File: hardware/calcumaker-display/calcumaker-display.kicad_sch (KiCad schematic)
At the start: 0 parts

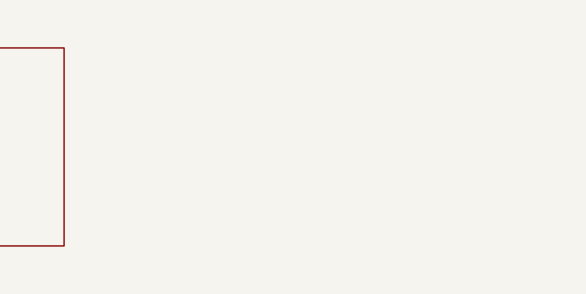
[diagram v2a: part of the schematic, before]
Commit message: Error handling: HP-style glass codes + DNP-optional aux OLED (display board)
Two layers, per design discussion:

ENGINE/APP — CalcError restructured: TypeError(&str) becomes Op(code, msg)
with class constructors at every site; code() gives the HP-16C-style glass
class (0 math domain, 1 register/flag, 2 bits/shift/word, 3 mode ranges,
4 too large, 5 no solution, 6 stack/entry, 7 dates, 8 statistics, 9 reserved
for crash recovery), text() the full string. App shows a transient 'Error N'
on the X row (cleared by the next key, like SHOW) and keeps the full text on
the status line — the duplicated error-string mapping in run_owned/flush is
now one report() helper. All of 'Error N' renders on the 7-seg. 211 tests.

HARDWARE — the aux OLED lands on the DISPLAY board (user decision): new
AuxDisplay sheet with J2, a 1x4 socket (PZ254V-11-04P C2691448) receiving a
standard 0.91in SSD1306 128x32 I2C module, DNP by default, hand-placed with
the THT digits. Interconnect grows 1x8 -> 1x10 (PZ254V-11-10P C492409, both
boards, pinout now ... 8=+3V3 9=SDA 10=SCL); I2C pull-ups R14/R15 4.7k on
the main board, DNP with the OLED. Both boards regenerate + check clean
(main 161, display 22 components). DESIGN.md documents the layered error
story and names the reusable 'DNP-optional aux' pattern; PARTS.md updated.

Co-Authored-By: Claude Fable 5 <noreply@anthropic.com>
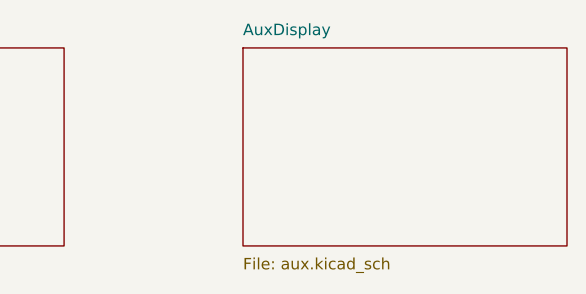
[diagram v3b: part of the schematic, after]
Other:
- added sheet AuxDisplay (aux.kicad_sch)
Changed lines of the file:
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@@
+		)
+	)
+	(sheet
+		(at 152.40 40.64)
+		(size 36.00 22.00)
+		(fields_autoplaced yes)
+		(stroke (width 0.1524) (type solid))
+		(fill (color 0 0 0 0.0000))
+		(property "Sheetname" "AuxDisplay"
+			(at 152.40 39.37 0)
+			(effects (font (size 1.27 1.27)) (justify left bottom))
+		)
+		(property "Sheetfile" "aux.kicad_sch"
+			(at 152.40 63.91 0)
+			(effects (font (size 1.27 1.27)) (justify left top))
 		)
 	)

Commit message: hardware: 3-board split (MCU + keyboard + display), wired display, real connectors
Split the single logic board into three, wire the display as a KiCad
multi-channel design, and settle every interconnect on real, in-stock parts.

Three-board split (was two):
- Rename calcumaker-main -> calcumaker-mcu (brain/PSU logic board).
- New calcumaker-keyboard board: 50-key Cherry MX matrix + its own
  STM32G031K8U6 scanner (LCSC C432207, UFQFPN-32) + annunciator LEDs,
  mezzanine-stacked above the MCU board. Keyscanning is off the main board;
  only an I2C + UART link + KB_IRQ wake + power cross the mezzanine.

Display board (calcumaker-display):
- Corrected FJ5161AH to a SINGLE-digit 0.56" common-cathode part (C8093) --
  it is NOT a 4-digit module; 48 single digits (16/row x 3), authored symbol
  + 0.56" LTS6760 land. The old 4-digit CC56-12 mapping (and its 3D model)
  was the phantom "clock colon".
- Rebuilt as a KiCad multi-channel design: one reusable display_row.kicad_sch
  (1 TM1640 + 16 digits, fully wired) instantiated x3. Extended kschgen.py
  with wiring primitives + reused-sheet (multi-channel) support.

Connectors (real, verified LCSC / DigiKey parts):
- Display link -> 0.5mm 12P FFC: AFC01-S12FCA-00 (LCSC C262661) on both
  boards; cable = GCT FFC05-TIN 05-12-A-<len>-A-4-06-4-T (DigiKey accessory,
  length TBD). +5V/GND conductors doubled for the display LED current.
- Keyboard mezzanine -> low-profile Hirose DF40 (0.4mm, 2x5, 1.5mm stack):
  DF40C-10DS (C424636) + DF40C-10DP (C424635) -- dedicated KiCad footprint
  + 3D model, unlike the datasheet-less generic parts first considered.

Low-power & wake documented (two Stop domains; keypress -> G0 EXTI wake ->
KB_IRQ -> U575 WKUP; G0 also wakes on I2C address-match). calcumaker-core
is unchanged -- App still consumes (row,col).

All three boards generate + pass the structure check (mcu 52 / keyboard 119 /
display 60 components, all footprints assigned, no duplicate refs). Docs
(DESIGN.md, PARTS.md incl. a Non-B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
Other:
- removed sheet Display
- added sheet Row1 (display_row.kicad_sch)
- added sheet Row2 (display_row.kicad_sch)
- added sheet Row3 (display_row.kicad_sch)
- note added: "Calcumaker 16 — Display (MULTI-CHANNEL). Row1/2/3 are three instances of ONE reusable sheet (display_row.kicad_sch). Shared bus is carried on global nets +5V / GND / DISP_CLK; each row's serial data DIN is a hierarchical pin fed by DIN1/DIN2/DIN3 from the interconnect. Top row (Row3 / U3 / DS33-48) is optional -> 2- or 3-row build."
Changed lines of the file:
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@@
 	(title_block
 		(title "Calcumaker 16 — Display")
-		(date "2026-06-21")
-		(rev "0.1")
+		(date "2026-07-04")
+		(rev "0.2")
 		(company "calcumaker authors")
 		(comment 1 "Programmer's/technical arbitrary-precision RPN calculator")
-		(comment 2 "Display board: 7-seg RPN stack + driver + interconnect (DRAFT)")
+		(comment 2 "Display board: multi-channel 7-seg RPN stack + drivers + interconnect (DRAFT)")
 	)
 	(sheet
-		(at 40.64 40.64)
-		(size 36.00 22.00)
+		(at 71.1200 30.4800)
+		(size 60.9600 20.3200)
 		(fields_autoplaced yes)
 		(stroke (width 0.1524) (type solid))
 		(fill (color 0 0 0 0.0000))
-		(property "Sheetname" "Display"
-			(at 40.64 39.37 0)
+		(property "Sheetname" "Row1"
+			(at 71.1200 29.2100 0)
 			(effects (font (size 1.27 1.27)) (justify left bottom))
 		)
-		(property "Sheetfile" "display.kicad_sch"
-			(at 40.64 63.91 0)
+		(property "Sheetfile" "display_row.kicad_sch"
+			(at 71.1200 52.0700 0)
+			(effects (font (size 1.27 1.27)) (justify left top))
+		)
+		(pin "DIN" input
+			(at 71.1200 40.6400 180)
+			(effects (font (size 1.27 1.27)) (justify left))
+		)
+	)
+	(sheet
+		(at 71.1200 60.9600)
+		(size 60.9600 20.3200)
+		(fields_autoplaced yes)
+		(stroke (width 0.1524) (type solid))
+		(fill (color 0 0 0 0.0000))
+		(property "Sheetname" "Row2"
+			(at 71.1200 59.6900 0)
+			(effects (font (size 1.27 1.27)) (justify left bottom))
+		)
+		(property "Sheetfile" "display_row.kicad_sch"
+			(at 71.1200 82.5500 0)
+			(effects (font (size 1.27 1.27)) (justify left top))
+		)
+		(pin "DIN" input
+			(at 71.1200 71.1200 180)
+			(effects (font (size 1.27 1.27)) (justify left))
+		)
+	)
+	(sheet
+		(at 71.1200 91.4400)
+		(size 60.9600 20.3200)
+		(fields_autoplaced yes)
+		(stroke (width 0.1524) (type solid))
+		(fill (color 0 0 0 0.0000))
+		(property "Sheetname" "Row3"
+			(at 71.1200 90.1700 0)
+			(effects (font (size 1.27 1.27)) (justify left bottom))
+		)
+		(property "Sheetfile" "display_row.kicad_sch"
+			(at 71.1200 113.0300 0)
+			(effects (font (size 1.27 1.27)) (justify left top))
+		)
+		(pin "DIN" input
+			(at 71.1200 101.6000 180)
+			(effects (font (size 1.27 1.27)) (justify left))
+		)
+	)
+	(sheet
+		(at 162.5600 30.4800)
+		(size 50.8000 20.3200)
+		(fields_autoplaced yes)
+		(stroke (width 0.1524) (type solid))
+		(fill (color 0 0 0 0.0000))
+		(property "Sheetname" "Interconnect"
+			(at 162.5600 29.2100 0)
+			(effects (font (size 1.27 1.27)) (justify left bottom))
+		)
+		(property "Sheetfile" "interconnect.kicad_sch"
+			(at 162.5600 52.0700 0)
 			(effects (font (size 1.27 1.27)) (justify left top))
 		)
 	)
 	(sheet
-		(at 96.52 40.64)
-		(size 36.00 22.00)
-		(fields_autoplaced yes)
-		(stroke (width 0.1524) (type solid))
-		(fill (color 0 0 0 0.0000))
-		(property "Sheetname" "Interconnect"
-			(at 96.52 39.37 0)
-			(effects (font (size 1.27 1.27)) (justify left bottom))
-		)
-		(property "Sheetfile" "interconnect.kicad_sch"
-			(at 96.52 63.91 0)
-			(effects (font (size 1.27 1.27)) (justify left top))
-		)
-	)
-	(sheet
-		(at 152.40 40.64)
-		(size 36.00 22.00)
+		(at 162.5600 60.9600)
+		(size 50.8000 20.3200)
 		(fields_autoplaced yes)
 		(stroke (width 0.1524) (type solid))
 		(fill (color 0 0 0 0.0000))
 		(property "Sheetname" "AuxDisplay"
-			(at 152.40 39.37 0)
+			(at 162.5600 59.6900 0)
 			(effects (font (size 1.27 1.27)) (justify left bottom))
 		)
 		(property "Sheetfile" "aux.kicad_sch"
-			(at 152.40 63.91 0)
+			(at 162.5600 82.5500 0)
 			(effects (font (size 1.27 1.27)) (justify left top))
 		)
 	)
+	(wire (pts (xy 71.1200 40.6400) (xy 63.5000 40.6400))
+		(stroke (width 0) (type default))
+	)
+	(global_label "DIN1"
+		(shape output)
+		(at 63.5000 40.6400 180)
+		(fields_autoplaced yes)
+		(effects (font (size 1.27 1.27)) (justify left))
+	)
+	(wire (pts (xy 71.1200 71.1200) (xy 63.5000 71.1200))
+		(stroke (width 0) (type default))
+	)
+	(global_label "DIN2"
+		(shape output)
+		(at 63.5000 71.1200 180)
+		(fields_autoplaced yes)
+		(effects (font (size 1.27 1.27)) (justify left))
+	)
+	(wire (pts (xy 71.1200 101.6000) (xy 63.5000 101.6000))
+		(stroke (width 0) (type default))
+	)
+	(global_label "DIN3"
+		(shape output)
+		(at 63.5000 101.6000 180)
+		(fields_autoplaced yes)
+		(effects (font (size 1.27 1.27)) (justify left))
+	)
+	(text "Calcumaker 16 — Display (MULTI-CHANNEL). Row1/2/3 are three instances of ONE reusable sheet (display_row.kicad_sch). Shared bus is carried on global nets +5V / GND / DISP_CLK; each row's serial data DIN is a hierarchical pin fed by DIN1/DIN2/DIN3 from the interconnect. Top row (Row3 / U3 / DS33-48) is optional -> 2- or 3-row build."
+		(exclude_from_sim no)
+		(at 20.00 105.00 0)
+		(effects (font (size 1.5 1.5)) (justify left top))
+	)
 	(sheet_instances

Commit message: hardware: MCU -> STM32U575RGT6 (LQFP-64) + 4MB QSPI flash; monospace wiring notes
MCU package + external flash
- Swap U1 STM32U575ZGT6 (LQFP-144) -> STM32U575RGT6 (LQFP-64, LCSC C5270980).
  The firmware links at ~323 KB so 1 MB flash is ample (~3x headroom), and with
  the key matrix scanned off-board the LQFP-64 has enough GPIO — smaller/cheaper.
- Correct the flash size everywhere: the STM32 `G` code = 1 MB (not 2 MB; the
  `I` parts are 2 MB). memory.x FLASH 2048K -> 1024K; .cargo runner -> RGTx.
- Add U7 W25Q32JVSSIQ, a 4 MB (32 Mbit) quad-SPI NOR (LCSC C179173, SOIC-8) on
  OCTOSPI1 as a new QSPIFlash sheet (+ R9 CS# pull-up + C26 decoupling) for
  memory-mapped (XIP) constants + state/program storage.
- mcu board 52 -> 55 components / 7 sheets. Docs (DESIGN.md, PARTS.md, READMEs,
  CLAUDE/AGENTS) updated; availability ladder now lists RGT6/VGT6/ZGT6.

Monospace, multi-line schematic wiring notes
- kschgen text_note() now renders notes in a monospace font (Courier New) so
  tables/columns line up; add note_block() + pin_table() helpers.
- Reformat all 14 per-sheet notes into titled, multi-line, aligned blocks —
  connector pinouts as PIN/SIGNAL tables, power/MCU sheets as wiring blocks.

The regenerated schematics carry both changes, so this is one commit. All three
boards regenerate + pass the structure check (mcu 55 / keyboard 119 / display
60, no duplicate refs).

Co-Authored-By: Claude Opus 4.8 (1M context) <noreply@anthropic.com>
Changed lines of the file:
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@@
 		(exclude_from_sim no)
 		(at 20.00 105.00 0)
-		(effects (font (size 1.5 1.5)) (justify left top))
+		(effects (font (face "Courier New") (size 1.27 1.27)) (justify left top))
 	)
 	(sheet_instances

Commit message: hardware: unified SPI display-module interface + RGB dot-matrix board
Make the display a swappable module on ONE technology-agnostic connector
(mirrors the keyboard-G0 pattern): the MCU board speaks a single SPI
"display intent" bus and each display board carries its own MCU that
renders locally. Two interchangeable modules on the same 12-pin FFC.

- calcumaker-matrix (NEW): full-color RGB dot matrix, 96x24 = 2304x 1mm
  XL-1010RGBC-2812B-S (C51900942) driven by an RP2040 (PIO). Nested
  multi-channel: led_cluster (8x8) x12 -> led_row (768px chain) x3.
  Dedicated VSYS LED-power inlet keeps amps off the signal FFC. Authored
  the 1mm 1010 footprint; RP2040/flash/shifter symbols are stock.
- calcumaker-display (7-seg): retrofit to a smart module -- added an
  STM32G031 SPI slave, and moved the 5V boost (TPS61022) + 74HCT125
  shifter off the MCU board onto it. Interconnect reworked CLK/DIN -> SPI.
- calcumaker-mcu: DisplayIF simplified to the unified SPI connector +
  a 2-pin VSYS outlet for the matrix LED rail.

Unified pinout (mcu J3 / display J1 / matrix J1): VSYS,VSYS,GND,GND,+3V3,
SPI_SCLK,SPI_MOSI,SPI_CS,DISP_IRQ,DISP_NRST,DISP_BOOT,GND.

All boards generate + check clean (mcu 46 / keyboard 179 / display 77 /
matrix 2339, no dup refs). Docs (PARTS.md, DESIGN.md, Makefile) updated.
Firmware is deferred; the SPI contract is documented so it is unblocked.

Co-Authored-By: Claude Opus 4.8 (1M context) <noreply@anthropic.com>
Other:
- added sheet DispMCU (disp_mcu.kicad_sch)
- added sheet DispPower (disp_power.kicad_sch)
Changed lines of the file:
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@@
+		)
+	)
+	(sheet
+		(at 162.5600 91.4400)
+		(size 50.8000 20.3200)
+		(fields_autoplaced yes)
+		(stroke (width 0.1524) (type solid))
+		(fill (color 0 0 0 0.0000))
+		(property "Sheetname" "DispMCU"
+			(at 162.5600 90.1700 0)
+			(effects (font (size 1.27 1.27)) (justify left bottom))
+		)
+		(property "Sheetfile" "disp_mcu.kicad_sch"
+			(at 162.5600 113.0300 0)
+			(effects (font (size 1.27 1.27)) (justify left top))
+		)
+	)
+	(sheet
+		(at 162.5600 121.9200)
+		(size 50.8000 20.3200)
+		(fields_autoplaced yes)
+		(stroke (width 0.1524) (type solid))
+		(fill (color 0 0 0 0.0000))
+		(property "Sheetname" "DispPower"
+			(at 162.5600 120.6500 0)
+			(effects (font (size 1.27 1.27)) (justify left bottom))
+		)
+		(property "Sheetfile" "disp_power.kicad_sch"
+			(at 162.5600 143.5100 0)
+			(effects (font (size 1.27 1.27)) (justify left top))
 		)
 	)
